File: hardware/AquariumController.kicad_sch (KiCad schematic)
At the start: 17 parts, among them J1 Conn_01x07, J3 Conn_01x04, J4 Conn_01x04, U2 ULN2003, U3 74HC245, U4 ESP32-C3-WROOM-02-N4

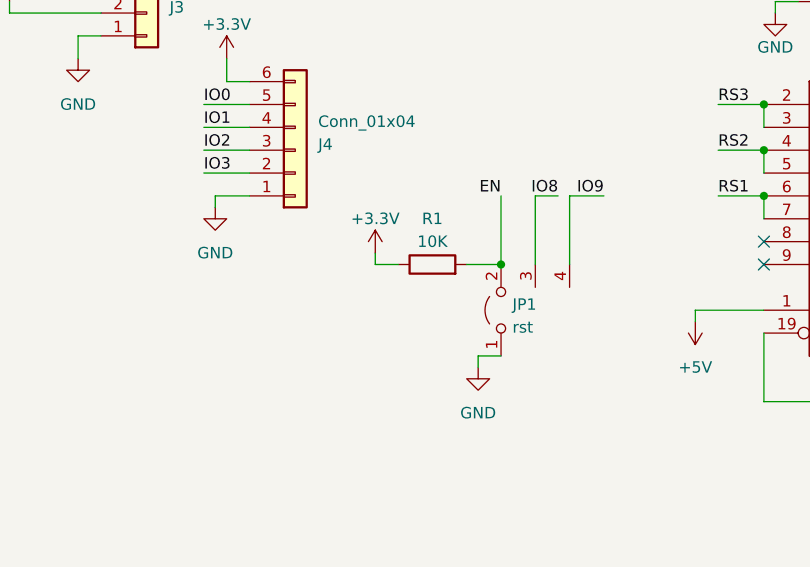
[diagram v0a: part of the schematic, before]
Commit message: added C13 on EN
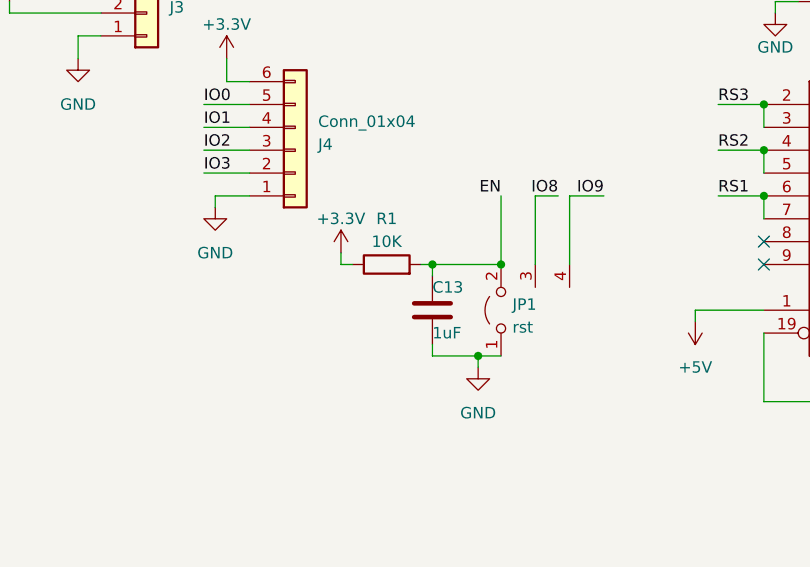
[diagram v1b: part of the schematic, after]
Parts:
- added C13: 1uF, Capacitor_SMD:C_0402_1005Metric, symbol Device:C
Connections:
- net EN: now also C13.2
- net GND: now also C13.1
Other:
- moved on the sheet: R1
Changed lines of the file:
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@@
   (junction (at 125.73 121.92) (diameter 0) (color 0 0 0 0)
   )
+  (junction (at 63.5 134.62) (diameter 0) (color 0 0 0 0)
+  )
   (junction (at 111.76 87.63) (diameter 0) (color 0 0 0 0)
   )
@@
   )
   (junction (at 100.33 127) (diameter 0) (color 0 0 0 0)
+  )
+  (junction (at 68.58 144.78) (diameter 0) (color 0 0 0 0)
   )
   (junction (at 125.73 127) (diameter 0) (color 0 0 0 0)
@@
     (stroke (width 0) (type default))
   )
-  (wire (pts (xy 59.69 134.62) (xy 57.15 134.62))
+  (wire (pts (xy 54.61 134.62) (xy 53.34 134.62))
     (stroke (width 0) (type default))
   )
@@
     (stroke (width 0) (type default))
   )
-  (wire (pts (xy 67.31 134.62) (xy 71.12 134.62))
+  (wire (pts (xy 62.23 134.62) (xy 63.5 134.62))
     (stroke (width 0) (type default))
   )
@@
     (stroke (width 0) (type default))
   )
+  (wire (pts (xy 63.5 144.78) (xy 68.58 144.78))
+    (stroke (width 0) (type default))
+  )
   (wire (pts (xy 78.74 127) (xy 82.55 127))
     (stroke (width 0) (type default))
@@
     (stroke (width 0) (type default))
   )
+  (wire (pts (xy 63.5 134.62) (xy 63.5 135.89))
+    (stroke (width 0) (type default))
+  )
   (wire (pts (xy 39.37 127) (xy 43.18 127))
     (stroke (width 0) (type default))
@@
     (stroke (width 0) (type default))
   )
-  (wire (pts (xy 57.15 134.62) (xy 57.15 133.35))
+  (wire (pts (xy 53.34 134.62) (xy 53.34 133.35))
+    (stroke (width 0) (type default))
+  )
+  (wire (pts (xy 63.5 143.51) (xy 63.5 144.78))
     (stroke (width 0) (type default))
   )
@@
   )
   (wire (pts (xy 139.7 63.5) (xy 146.05 63.5))
+    (stroke (width 0) (type default))
+  )
+  (wire (pts (xy 63.5 134.62) (xy 71.12 134.62))
     (stroke (width 0) (type default))
   )
@@
     )
   )
-  (symbol (lib_id "Device:R") (at 63.5 134.62 90) (unit 1)
-    (in_bom yes) (on_board yes) (dnp no) (fields_autoplaced)
-    (property "Reference" "R1" (at 63.5 129.54 90)
-      (effects (font (size 1.27 1.27)))
-    )
-    (property "Value" "10K" (at 63.5 132.08 90)
-      (effects (font (size 1.27 1.27)))
-    )
-    (property "Footprint" "Resistor_SMD:R_0402_1005Metric" (at 63.5 136.398 90)
-      (effects (font (size 1.27 1.27)) hide)
-    )
-    (property "Datasheet" "~" (at 63.5 134.62 0)
-      (effects (font (size 1.27 1.27)) hide)
-    )
-    (property "JLCPCB Part #" "C25744" (at 63.5 134.62 0)
+  (symbol (lib_id "Device:R") (at 58.42 134.62 90) (unit 1)
+    (in_bom yes) (on_board yes) (dnp no) (fields_autoplaced)
+    (property "Reference" "R1" (at 58.42 129.54 90)
+      (effects (font (size 1.27 1.27)))
+    )
+    (property "Value" "10K" (at 58.42 132.08 90)
+      (effects (font (size 1.27 1.27)))
+    )
+    (property "Footprint" "Resistor_SMD:R_0402_1005Metric" (at 58.42 136.398 90)
+      (effects (font (size 1.27 1.27)) hide)
+    )
+    (property "Datasheet" "~" (at 58.42 134.62 0)
+      (effects (font (size 1.27 1.27)) hide)
+    )
+    (property "JLCPCB Part #" "C25744" (at 58.42 134.62 0)
       (effects (font (size 1.27 1.27)) hide)
     )
@@
     )
   )
+  (symbol (lib_id "Device:C") (at 63.5 139.7 180) (unit 1)
+    (in_bom yes) (on_board yes) (dnp no)
+    (property "Reference" "C13" (at 63.5 137.16 0)
+      (effects (font (size 1.27 1.27)) (justify right))
+    )
+    (property "Value" "1uF" (at 63.5 142.24 0)
+      (effects (font (size 1.27 1.27)) (justify right))
+    )
+    (property "Footprint" "Capacitor_SMD:C_0402_1005Metric" (at 62.5348 135.89 0)
+      (effects (font (size 1.27 1.27)) hide)
+    )
+    (property "Datasheet" "~" (at 63.5 139.7 0)
+      (effects (font (size 1.27 1.27)) hide)
+    )
+    (property "JLCPCB Part #" "C52923" (at 63.5 139.7 0)
+      (effects (font (size 1.27 1.27)) hide)
+    )
+    (pin "1")
+    (pin "2")
+    (instances
+      (project "AquariumController"
+        (path "/75069d71-4fd1-4b49-820b-d8e60608591a"
+          (reference "C13") (unit 1)
+        )
+      )
+    )
+  )
   (symbol (lib_id "ProjectLibrary:Jumper_4_Open_Pin") (at 71.12 139.7 90) (unit 1)
     (in_bom yes) (on_board yes) (dnp no) (fields_autoplaced)
@@
     )
   )
-  (symbol (lib_id "power:+3.3V") (at 57.15 133.35 0) (unit 1)
-    (in_bom yes) (on_board yes) (dnp no) (fields_autoplaced)
-    (property "Reference" "#PWR029" (at 57.15 137.16 0)
-      (effects (font (size 1.27 1.27)) hide)
-    )
-    (property "Value" "+3.3V" (at 57.15 129.54 0)
-      (effects (font (size 1.27 1.27)))
-    )
-    (property "Footprint" "" (at 57.15 133.35 0)
-      (effects (font (size 1.27 1.27)) hide)
-    )
-    (property "Datasheet" "" (at 57.15 133.35 0)
-      (effects (font (size 1.27 1.27)) hide)
-    )
+  (symbol (lib_id "power:+3.3V") (at 53.34 133.35 0) (unit 1)
+    (in_bom yes) (on_board yes) (dnp no) (fields_autoplaced)
+    (property "Reference" "#PWR029" (at 53.34 137.16 0)
+      (effects (font (size 1.27 1.27)) hide)
+    )
+    (property "Value" "+3.3V" (at 53.34 129.54 0)
+      (effects (font (size 1.27 1.27)))
+    )
+    (property "Footprint" "" (at 53.34 133.35 0)
+      (effects (font (size 1.27 1.27)) hide)
+    )
+    (property "Datasheet" "" (at 53.34 133.35 0)
+      (effects (font (size 1.27 1.27)) hide)
+    )

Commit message: 7.0.1-> 7.0.2, varistor update from library, temporary disable SPICE model issue violation
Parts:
- J3, J4, JP1: now left out of the parts list
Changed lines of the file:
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@@
   )
   (symbol (lib_id "Connector_Generic:Conn_01x04") (at 31.75 106.68 0) (mirror x) (unit 1)
-    (in_bom yes) (on_board yes) (dnp no)
+    (in_bom no) (on_board yes) (dnp no)
     (property "Reference" "J3" (at 34.29 106.045 0)
       (effects (font (size 1.27 1.27)) (justify left))
@@
   )
   (symbol (lib_id "ProjectLibrary:Jumper_4_Open_Pin") (at 71.12 139.7 90) (unit 1)
-    (in_bom yes) (on_board yes) (dnp no) (fields_autoplaced)
+    (in_bom no) (on_board yes) (dnp no) (fields_autoplaced)
     (property "Reference" "JP1" (at 72.39 139.065 90)
       (effects (font (size 1.27 1.27)) (justify right))
@@
   )
   (symbol (lib_id "Connector_Generic:Conn_01x06") (at 48.26 121.92 0) (mirror x) (unit 1)
-    (in_bom yes) (on_board yes) (dnp no)
+    (in_bom no) (on_board yes) (dnp no)
     (property "Reference" "J4" (at 50.8 121.285 0)
       (effects (font (size 1.27 1.27)) (justify left))
